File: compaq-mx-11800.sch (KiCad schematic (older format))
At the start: 240 parts, among them J1 Conn_01x16_Female, J2 Conn_01x16_Female

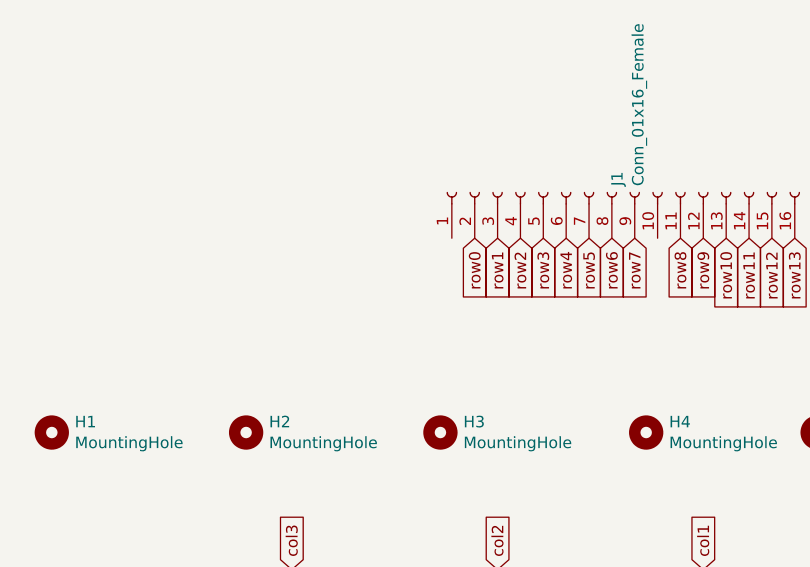
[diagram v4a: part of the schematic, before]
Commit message: add filled zones
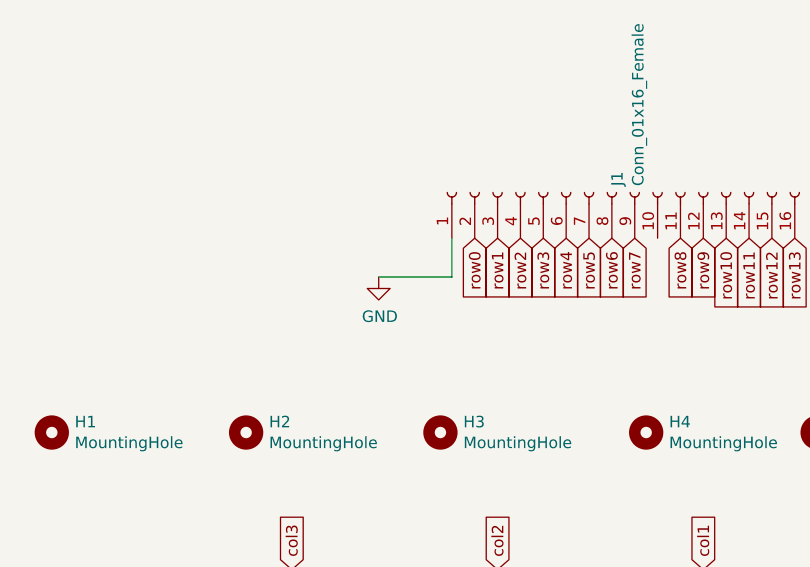
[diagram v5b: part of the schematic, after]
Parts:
- MX1, MX10, MX11, MX12, MX17, MX18, MX19, MX2, MX20, MX21, MX22, MX23, MX24, MX25, MX26, MX27, MX3, MX4, MX5, MX6, MX7, MX8, MX9: footprint MX_Only:MXOnly-1U-NoLED -> MX_Alps_Hybrid:MX-1U-NoLED
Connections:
- net labels added: GND
- wire segments 776 -> 778
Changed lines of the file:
@@
 F 0 "MX1" H 9083 8323 60  0000 C CNN
 F 1 "MX-NoLED" H 9083 8249 20  0000 C CNN
-F 2 "MX_Only:MXOnly-1U-NoLED" H 8425 8075 60  0001 C CNN
+F 2 "MX_Alps_Hybrid:MX-1U-NoLED" H 8425 8075 60  0001 C CNN
 F 3 "" H 8425 8075 60  0001 C CNN
 	1    9050 8100
@@
 F 0 "MX20" H 10883 9123 60  0000 C CNN
 F 1 "MX-NoLED" H 10883 9049 20  0000 C CNN
-F 2 "MX_Only:MXOnly-1U-NoLED" H 10225 8875 60  0001 C CNN
+F 2 "MX_Alps_Hybrid:MX-1U-NoLED" H 10225 8875 60  0001 C CNN
 F 3 "" H 10225 8875 60  0001 C CNN
 	1    10850 8900
@@
 F 0 "MX19" H 10433 9123 60  0000 C CNN
 F 1 "MX-NoLED" H 10433 9049 20  0000 C CNN
-F 2 "MX_Only:MXOnly-1U-NoLED" H 9775 8875 60  0001 C CNN
+F 2 "MX_Alps_Hybrid:MX-1U-NoLED" H 9775 8875 60  0001 C CNN
 F 3 "" H 9775 8875 60  0001 C CNN
 	1    10400 8900
@@
 F 0 "MX18" H 9983 9123 60  0000 C CNN
 F 1 "MX-NoLED" H 9983 9049 20  0000 C CNN
-F 2 "MX_Only:MXOnly-1U-NoLED" H 9325 8875 60  0001 C CNN
+F 2 "MX_Alps_Hybrid:MX-1U-NoLED" H 9325 8875 60  0001 C CNN
 F 3 "" H 9325 8875 60  0001 C CNN
 	1    9950 8900
@@
 F 0 "MX4" H 10883 8323 60  0000 C CNN
 F 1 "MX-NoLED" H 10883 8249 20  0000 C CNN
-F 2 "MX_Only:MXOnly-1U-NoLED" H 10225 8075 60  0001 C CNN
+F 2 "MX_Alps_Hybrid:MX-1U-NoLED" H 10225 8075 60  0001 C CNN
 F 3 "" H 10225 8075 60  0001 C CNN
 	1    10850 8100
@@
 F 0 "MX3" H 10433 8323 60  0000 C CNN
 F 1 "MX-NoLED" H 10433 8249 20  0000 C CNN
-F 2 "MX_Only:MXOnly-1U-NoLED" H 9775 8075 60  0001 C CNN
+F 2 "MX_Alps_Hybrid:MX-1U-NoLED" H 9775 8075 60  0001 C CNN
 F 3 "" H 9775 8075 60  0001 C CNN
 	1    10400 8100
@@
 F 0 "MX2" H 9983 8323 60  0000 C CNN
 F 1 "MX-NoLED" H 9983 8249 20  0000 C CNN
-F 2 "MX_Only:MXOnly-1U-NoLED" H 9325 8075 60  0001 C CNN
+F 2 "MX_Alps_Hybrid:MX-1U-NoLED" H 9325 8075 60  0001 C CNN
 F 3 "" H 9325 8075 60  0001 C CNN
 	1    9950 8100
@@
 F 0 "MX5" H 11333 8323 60  0000 C CNN
 F 1 "MX-NoLED" H 11333 8249 20  0000 C CNN
-F 2 "MX_Only:MXOnly-1U-NoLED" H 10675 8075 60  0001 C CNN
+F 2 "MX_Alps_Hybrid:MX-1U-NoLED" H 10675 8075 60  0001 C CNN
 F 3 "" H 10675 8075 60  0001 C CNN
 	1    11300 8100
@@
 F 0 "MX6" H 11783 8323 60  0000 C CNN
 F 1 "MX-NoLED" H 11783 8249 20  0000 C CNN
-F 2 "MX_Only:MXOnly-1U-NoLED" H 11125 8075 60  0001 C CNN
+F 2 "MX_Alps_Hybrid:MX-1U-NoLED" H 11125 8075 60  0001 C CNN
 F 3 "" H 11125 8075 60  0001 C CNN
 	1    11750 8100
@@
 F 0 "MX7" H 12233 8323 60  0000 C CNN
 F 1 "MX-NoLED" H 12233 8249 20  0000 C CNN
-F 2 "MX_Only:MXOnly-1U-NoLED" H 11575 8075 60  0001 C CNN
+F 2 "MX_Alps_Hybrid:MX-1U-NoLED" H 11575 8075 60  0001 C CNN
 F 3 "" H 11575 8075 60  0001 C CNN
 	1    12200 8100
@@
 F 0 "MX8" H 13133 8323 60  0000 C CNN
 F 1 "MX-NoLED" H 13133 8249 20  0000 C CNN
-F 2 "MX_Only:MXOnly-1U-NoLED" H 12475 8075 60  0001 C CNN
+F 2 "MX_Alps_Hybrid:MX-1U-NoLED" H 12475 8075 60  0001 C CNN
 F 3 "" H 12475 8075 60  0001 C CNN
 	1    13100 8100
@@
 F 0 "MX9" H 13583 8323 60  0000 C CNN
 F 1 "MX-NoLED" H 13583 8249 20  0000 C CNN
-F 2 "MX_Only:MXOnly-1U-NoLED" H 12925 8075 60  0001 C CNN
+F 2 "MX_Alps_Hybrid:MX-1U-NoLED" H 12925 8075 60  0001 C CNN
 F 3 "" H 12925 8075 60  0001 C CNN
 	1    13550 8100
@@
 F 0 "MX21" H 11333 9123 60  0000 C CNN
 F 1 "MX-NoLED" H 11333 9049 20  0000 C CNN
-F 2 "MX_Only:MXOnly-1U-NoLED" H 10675 8875 60  0001 C CNN
+F 2 "MX_Alps_Hybrid:MX-1U-NoLED" H 10675 8875 60  0001 C CNN
 F 3 "" H 10675 8875 60  0001 C CNN
 	1    11300 8900
@@
 F 0 "MX22" H 11783 9123 60  0000 C CNN
 F 1 "MX-NoLED" H 11783 9049 20  0000 C CNN
-F 2 "MX_Only:MXOnly-1U-NoLED" H 11125 8875 60  0001 C CNN
+F 2 "MX_Alps_Hybrid:MX-1U-NoLED" H 11125 8875 60  0001 C CNN
 F 3 "" H 11125 8875 60  0001 C CNN
 	1    11750 8900
@@
 F 0 "MX23" H 12233 9123 60  0000 C CNN
 F 1 "MX-NoLED" H 12233 9049 20  0000 C CNN
-F 2 "MX_Only:MXOnly-1U-NoLED" H 11575 8875 60  0001 C CNN
+F 2 "MX_Alps_Hybrid:MX-1U-NoLED" H 11575 8875 60  0001 C CNN
 F 3 "" H 11575 8875 60  0001 C CNN
 	1    12200 8900
@@
 F 0 "MX24" H 13133 9123 60  0000 C CNN
 F 1 "MX-NoLED" H 13133 9049 20  0000 C CNN
-F 2 "MX_Only:MXOnly-1U-NoLED" H 12475 8875 60  0001 C CNN
+F 2 "MX_Alps_Hybrid:MX-1U-NoLED" H 12475 8875 60  0001 C CNN
 F 3 "" H 12475 8875 60  0001 C CNN
 	1    13100 8900
@@
 F 0 "MX25" H 13583 9123 60  0000 C CNN
 F 1 "MX-NoLED" H 13583 9049 20  0000 C CNN
-F 2 "MX_Only:MXOnly-1U-NoLED" H 12925 8875 60  0001 C CNN
+F 2 "MX_Alps_Hybrid:MX-1U-NoLED" H 12925 8875 60  0001 C CNN
 F 3 "" H 12925 8875 60  0001 C CNN
 	1    13550 8900
@@
 F 0 "MX26" H 14033 9123 60  0000 C CNN
 F 1 "MX-NoLED" H 14033 9049 20  0000 C CNN
-F 2 "MX_Only:MXOnly-1U-NoLED" H 13375 8875 60  0001 C CNN
+F 2 "MX_Alps_Hybrid:MX-1U-NoLED" H 13375 8875 60  0001 C CNN
 F 3 "" H 13375 8875 60  0001 C CNN
 	1    14000 8900
@@
 F 0 "MX10" H 14033 8323 60  0000 C CNN
 F 1 "MX-NoLED" H 14033 8249 20  0000 C CNN
-F 2 "MX_Only:MXOnly-1U-NoLED" H 13375 8075 60  0001 C CNN
+F 2 "MX_Alps_Hybrid:MX-1U-NoLED" H 13375 8075 60  0001 C CNN
 F 3 "" H 13375 8075 60  0001 C CNN
 	1    14000 8100
@@
 F 0 "MX11" H 14483 8323 60  0000 C CNN
 F 1 "MX-NoLED" H 14483 8249 20  0000 C CNN
-F 2 "MX_Only:MXOnly-1U-NoLED" H 13825 8075 60  0001 C CNN
+F 2 "MX_Alps_Hybrid:MX-1U-NoLED" H 13825 8075 60  0001 C CNN
 F 3 "" H 13825 8075 60  0001 C CNN
 	1    14450 8100
@@
 F 0 "MX27" H 14483 9123 60  0000 C CNN
 F 1 "MX-NoLED" H 14483 9049 20  0000 C CNN
-F 2 "MX_Only:MXOnly-1U-NoLED" H 13825 8875 60  0001 C CNN
+F 2 "MX_Alps_Hybrid:MX-1U-NoLED" H 13825 8875 60  0001 C CNN
 F 3 "" H 13825 8875 60  0001 C CNN
 	1    14450 8900
@@
 F 0 "MX12" H 14983 8323 60  0000 C CNN
 F 1 "MX-NoLED" H 14983 8249 20  0000 C CNN
-F 2 "MX_Only:MXOnly-1U-NoLED" H 14325 8075 60  0001 C CNN
+F 2 "MX_Alps_Hybrid:MX-1U-NoLED" H 14325 8075 60  0001 C CNN
 F 3 "" H 14325 8075 60  0001 C CNN
 	1    14950 8100
@@
 F 0 "MX17" H 18283 9273 60  0000 C CNN
 F 1 "MX-NoLED" H 18283 9199 20  0000 C CNN
-F 2 "MX_Only:MXOnly-1U-NoLED" H 17625 9025 60  0001 C CNN
+F 2 "MX_Alps_Hybrid:MX-1U-NoLED" H 17625 9025 60  0001 C CNN
 F 3 "" H 17625 9025 60  0001 C CNN
 	1    18250 9050
@@
 Wire Wire Line
 	8900 11100 8900 11200
+$Comp
+L power:GND #PWR0101
+U 1 1 61E256F8
+P 9630 6470
+F 0 "#PWR0101" H 9630 6220 50  0001 C CNN
+F 1 "GND" H 9635 6297 50  0000 C CNN
+F 2 "" H 9630 6470 50  0001 C CNN
+F 3 "" H 9630 6470 50  0001 C CNN
+	1    9630 6470
+	1    0    0    -1
+$EndComp
+Wire Wire Line
+	9950 6300 9950 6470
+Wire Wire Line
+	9950 6470 9630 6470
 $EndSCHEMATC

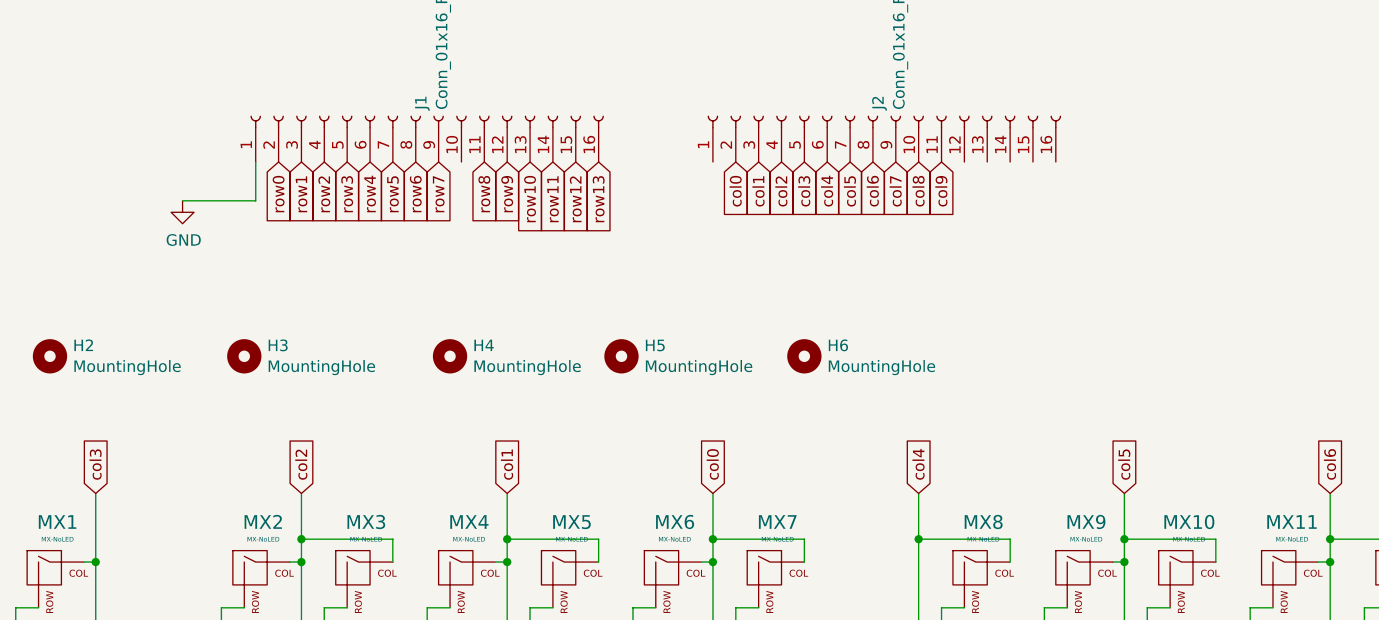
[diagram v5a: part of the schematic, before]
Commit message: add ground pins
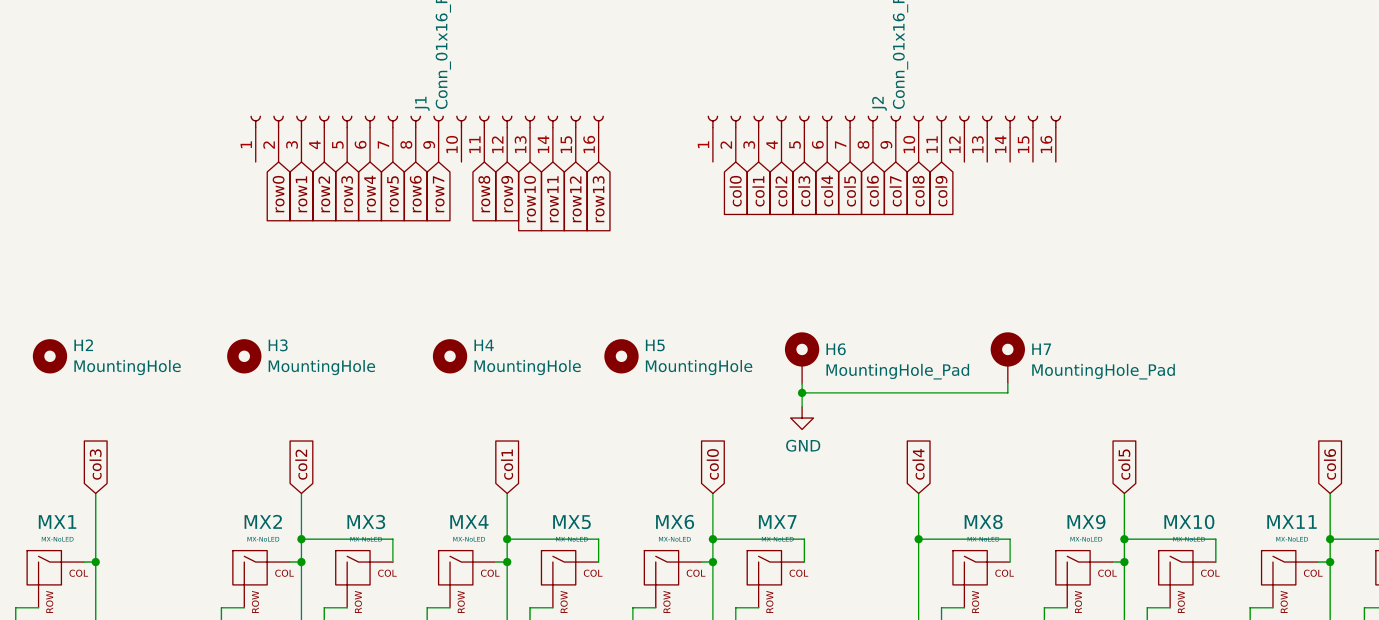
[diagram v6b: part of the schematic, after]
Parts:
- removed H6: MountingHole, Keebio-Parts:SolidCopper, symbol Mechanical:MountingHole
- added H6, H7: MountingHole_Pad, Keebio-Parts:SolidCopper, symbol Mechanical:MountingHole_Pad
- MX1, MX10, MX11, MX12, MX17, MX18, MX19, MX2, MX20, MX21, MX22, MX23, MX24, MX25, MX26, MX27, MX3, MX4, MX5, MX6, MX7, MX8, MX9: footprint MX_Alps_Hybrid:MX-1U-NoLED -> MX_Only:MXOnly-1U-NoLED
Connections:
- wire segments 778 -> 780
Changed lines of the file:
@@
 F 0 "MX1" H 9083 8323 60  0000 C CNN
 F 1 "MX-NoLED" H 9083 8249 20  0000 C CNN
-F 2 "MX_Alps_Hybrid:MX-1U-NoLED" H 8425 8075 60  0001 C CNN
+F 2 "MX_Only:MXOnly-1U-NoLED" H 8425 8075 60  0001 C CNN
 F 3 "" H 8425 8075 60  0001 C CNN
 	1    9050 8100
@@
 F 0 "MX20" H 10883 9123 60  0000 C CNN
 F 1 "MX-NoLED" H 10883 9049 20  0000 C CNN
-F 2 "MX_Alps_Hybrid:MX-1U-NoLED" H 10225 8875 60  0001 C CNN
+F 2 "MX_Only:MXOnly-1U-NoLED" H 10225 8875 60  0001 C CNN
 F 3 "" H 10225 8875 60  0001 C CNN
 	1    10850 8900
@@
 F 0 "MX19" H 10433 9123 60  0000 C CNN
 F 1 "MX-NoLED" H 10433 9049 20  0000 C CNN
-F 2 "MX_Alps_Hybrid:MX-1U-NoLED" H 9775 8875 60  0001 C CNN
+F 2 "MX_Only:MXOnly-1U-NoLED" H 9775 8875 60  0001 C CNN
 F 3 "" H 9775 8875 60  0001 C CNN
 	1    10400 8900
@@
 F 0 "MX18" H 9983 9123 60  0000 C CNN
 F 1 "MX-NoLED" H 9983 9049 20  0000 C CNN
-F 2 "MX_Alps_Hybrid:MX-1U-NoLED" H 9325 8875 60  0001 C CNN
+F 2 "MX_Only:MXOnly-1U-NoLED" H 9325 8875 60  0001 C CNN
 F 3 "" H 9325 8875 60  0001 C CNN
 	1    9950 8900
@@
 F 0 "MX4" H 10883 8323 60  0000 C CNN
 F 1 "MX-NoLED" H 10883 8249 20  0000 C CNN
-F 2 "MX_Alps_Hybrid:MX-1U-NoLED" H 10225 8075 60  0001 C CNN
+F 2 "MX_Only:MXOnly-1U-NoLED" H 10225 8075 60  0001 C CNN
 F 3 "" H 10225 8075 60  0001 C CNN
 	1    10850 8100
@@
 F 0 "MX3" H 10433 8323 60  0000 C CNN
 F 1 "MX-NoLED" H 10433 8249 20  0000 C CNN
-F 2 "MX_Alps_Hybrid:MX-1U-NoLED" H 9775 8075 60  0001 C CNN
+F 2 "MX_Only:MXOnly-1U-NoLED" H 9775 8075 60  0001 C CNN
 F 3 "" H 9775 8075 60  0001 C CNN
 	1    10400 8100
@@
 F 0 "MX2" H 9983 8323 60  0000 C CNN
 F 1 "MX-NoLED" H 9983 8249 20  0000 C CNN
-F 2 "MX_Alps_Hybrid:MX-1U-NoLED" H 9325 8075 60  0001 C CNN
+F 2 "MX_Only:MXOnly-1U-NoLED" H 9325 8075 60  0001 C CNN
 F 3 "" H 9325 8075 60  0001 C CNN
 	1    9950 8100
@@
 F 0 "MX5" H 11333 8323 60  0000 C CNN
 F 1 "MX-NoLED" H 11333 8249 20  0000 C CNN
-F 2 "MX_Alps_Hybrid:MX-1U-NoLED" H 10675 8075 60  0001 C CNN
+F 2 "MX_Only:MXOnly-1U-NoLED" H 10675 8075 60  0001 C CNN
 F 3 "" H 10675 8075 60  0001 C CNN
 	1    11300 8100
@@
 F 0 "MX6" H 11783 8323 60  0000 C CNN
 F 1 "MX-NoLED" H 11783 8249 20  0000 C CNN
-F 2 "MX_Alps_Hybrid:MX-1U-NoLED" H 11125 8075 60  0001 C CNN
+F 2 "MX_Only:MXOnly-1U-NoLED" H 11125 8075 60  0001 C CNN
 F 3 "" H 11125 8075 60  0001 C CNN
 	1    11750 8100
@@
 F 0 "MX7" H 12233 8323 60  0000 C CNN
 F 1 "MX-NoLED" H 12233 8249 20  0000 C CNN
-F 2 "MX_Alps_Hybrid:MX-1U-NoLED" H 11575 8075 60  0001 C CNN
+F 2 "MX_Only:MXOnly-1U-NoLED" H 11575 8075 60  0001 C CNN
 F 3 "" H 11575 8075 60  0001 C CNN
 	1    12200 8100
@@
 F 0 "MX8" H 13133 8323 60  0000 C CNN
 F 1 "MX-NoLED" H 13133 8249 20  0000 C CNN
-F 2 "MX_Alps_Hybrid:MX-1U-NoLED" H 12475 8075 60  0001 C CNN
+F 2 "MX_Only:MXOnly-1U-NoLED" H 12475 8075 60  0001 C CNN
 F 3 "" H 12475 8075 60  0001 C CNN
 	1    13100 8100
@@
 F 0 "MX9" H 13583 8323 60  0000 C CNN
 F 1 "MX-NoLED" H 13583 8249 20  0000 C CNN
-F 2 "MX_Alps_Hybrid:MX-1U-NoLED" H 12925 8075 60  0001 C CNN
+F 2 "MX_Only:MXOnly-1U-NoLED" H 12925 8075 60  0001 C CNN
 F 3 "" H 12925 8075 60  0001 C CNN
 	1    13550 8100
@@
 F 0 "MX21" H 11333 9123 60  0000 C CNN
 F 1 "MX-NoLED" H 11333 9049 20  0000 C CNN
-F 2 "MX_Alps_Hybrid:MX-1U-NoLED" H 10675 8875 60  0001 C CNN
+F 2 "MX_Only:MXOnly-1U-NoLED" H 10675 8875 60  0001 C CNN
 F 3 "" H 10675 8875 60  0001 C CNN
 	1    11300 8900
@@
 F 0 "MX22" H 11783 9123 60  0000 C CNN
 F 1 "MX-NoLED" H 11783 9049 20  0000 C CNN
-F 2 "MX_Alps_Hybrid:MX-1U-NoLED" H 11125 8875 60  0001 C CNN
+F 2 "MX_Only:MXOnly-1U-NoLED" H 11125 8875 60  0001 C CNN
 F 3 "" H 11125 8875 60  0001 C CNN
 	1    11750 8900
@@
 F 0 "MX23" H 12233 9123 60  0000 C CNN
 F 1 "MX-NoLED" H 12233 9049 20  0000 C CNN
-F 2 "MX_Alps_Hybrid:MX-1U-NoLED" H 11575 8875 60  0001 C CNN
+F 2 "MX_Only:MXOnly-1U-NoLED" H 11575 8875 60  0001 C CNN
 F 3 "" H 11575 8875 60  0001 C CNN
 	1    12200 8900
@@
 F 0 "MX24" H 13133 9123 60  0000 C CNN
 F 1 "MX-NoLED" H 13133 9049 20  0000 C CNN
-F 2 "MX_Alps_Hybrid:MX-1U-NoLED" H 12475 8875 60  0001 C CNN
+F 2 "MX_Only:MXOnly-1U-NoLED" H 12475 8875 60  0001 C CNN
 F 3 "" H 12475 8875 60  0001 C CNN
 	1    13100 8900
@@
 F 0 "MX25" H 13583 9123 60  0000 C CNN
 F 1 "MX-NoLED" H 13583 9049 20  0000 C CNN
-F 2 "MX_Alps_Hybrid:MX-1U-NoLED" H 12925 8875 60  0001 C CNN
+F 2 "MX_Only:MXOnly-1U-NoLED" H 12925 8875 60  0001 C CNN
 F 3 "" H 12925 8875 60  0001 C CNN
 	1    13550 8900
@@
 F 0 "MX26" H 14033 9123 60  0000 C CNN
 F 1 "MX-NoLED" H 14033 9049 20  0000 C CNN
-F 2 "MX_Alps_Hybrid:MX-1U-NoLED" H 13375 8875 60  0001 C CNN
+F 2 "MX_Only:MXOnly-1U-NoLED" H 13375 8875 60  0001 C CNN
 F 3 "" H 13375 8875 60  0001 C CNN
 	1    14000 8900
@@
 F 0 "MX10" H 14033 8323 60  0000 C CNN
 F 1 "MX-NoLED" H 14033 8249 20  0000 C CNN
-F 2 "MX_Alps_Hybrid:MX-1U-NoLED" H 13375 8075 60  0001 C CNN
+F 2 "MX_Only:MXOnly-1U-NoLED" H 13375 8075 60  0001 C CNN
 F 3 "" H 13375 8075 60  0001 C CNN
 	1    14000 8100
@@
 F 0 "MX11" H 14483 8323 60  0000 C CNN
 F 1 "MX-NoLED" H 14483 8249 20  0000 C CNN
-F 2 "MX_Alps_Hybrid:MX-1U-NoLED" H 13825 8075 60  0001 C CNN
+F 2 "MX_Only:MXOnly-1U-NoLED" H 13825 8075 60  0001 C CNN
 F 3 "" H 13825 8075 60  0001 C CNN
 	1    14450 8100
@@
 F 0 "MX27" H 14483 9123 60  0000 C CNN
 F 1 "MX-NoLED" H 14483 9049 20  0000 C CNN
-F 2 "MX_Alps_Hybrid:MX-1U-NoLED" H 13825 8875 60  0001 C CNN
+F 2 "MX_Only:MXOnly-1U-NoLED" H 13825 8875 60  0001 C CNN
 F 3 "" H 13825 8875 60  0001 C CNN
 	1    14450 8900
@@
 F 0 "MX12" H 14983 8323 60  0000 C CNN
 F 1 "MX-NoLED" H 14983 8249 20  0000 C CNN
-F 2 "MX_Alps_Hybrid:MX-1U-NoLED" H 14325 8075 60  0001 C CNN
+F 2 "MX_Only:MXOnly-1U-NoLED" H 14325 8075 60  0001 C CNN
 F 3 "" H 14325 8075 60  0001 C CNN
 	1    14950 8100
@@
 	9250 8050 9250 9950
 $Comp
-L Mechanical:MountingHole H6
-U 1 1 61D29BE7
-P 12350 7150
-F 0 "H6" H 12450 7196 50  0000 L CNN
-F 1 "MountingHole" H 12450 7105 50  0000 L CNN
-F 2 "Keebio-Parts:SolidCopper" H 12350 7150 50  0001 C CNN
-F 3 "~" H 12350 7150 50  0001 C CNN
-	1    12350 7150
-	1    0    0    -1
-$EndComp
-$Comp
 L Mechanical:MountingHole H5
 U 1 1 61CD4313
@@
 F 0 "MX17" H 18283 9273 60  0000 C CNN
 F 1 "MX-NoLED" H 18283 9199 20  0000 C CNN
-F 2 "MX_Alps_Hybrid:MX-1U-NoLED" H 17625 9025 60  0001 C CNN
+F 2 "MX_Only:MXOnly-1U-NoLED" H 17625 9025 60  0001 C CNN
 F 3 "" H 17625 9025 60  0001 C CNN
 	1    18250 9050
@@
 	8900 11100 8900 11200
 $Comp
-L power:GND #PWR0101
-U 1 1 61E256F8
-P 9630 6470
-F 0 "#PWR0101" H 9630 6220 50  0001 C CNN
-F 1 "GND" H 9635 6297 50  0000 C CNN
-F 2 "" H 9630 6470 50  0001 C CNN
-F 3 "" H 9630 6470 50  0001 C CNN
-	1    9630 6470
+L Mechanical:MountingHole_Pad H7
+U 1 1 620D9A4A
+P 13240 7170
+F 0 "H7" H 13340 7219 50  0000 L CNN
+F 1 "MountingHole_Pad" H 13340 7128 50  0000 L CNN
+F 2 "Keebio-Parts:SolidCopper" H 13240 7170 50  0001 C CNN
+F 3 "~" H 13240 7170 50  0001 C CNN
+	1    13240 7170
+	1    0    0    -1
+$EndComp
+$Comp
+L power:GND #PWR0102
+U 1 1 62315AC5
+P 12340 7370
+F 0 "#PWR0102" H 12340 7120 50  0001 C CNN
+F 1 "GND" H 12345 7197 50  0000 C CNN
+F 2 "" H 12340 7370 50  0001 C CNN
+F 3 "" H 12340 7370 50  0001 C CNN
+	1    12340 7370
 	1    0    0    -1
 $EndComp
+$Comp
+L Mechanical:MountingHole_Pad H6
+U 1 1 62315ACB
+P 12340 7170
+F 0 "H6" H 12440 7219 50  0000 L CNN
+F 1 "MountingHole_Pad" H 12440 7128 50  0000 L CNN
+F 2 "Keebio-Parts:SolidCopper" H 12340 7170 50  0001 C CNN
+F 3 "~" H 12340 7170 50  0001 C CNN
+	1    12340 7170
+	1    0    0    -1
+$EndComp
+Wire Wire Line
+	12340 7270 12340 7310
+Wire Wire Line
+	13240 7270 13240 7310
 Wire Wire Line
-	9950 6300 9950 6470
+	13240 7310 12340 7310
+Connection ~ 12340 7310
 Wire Wire Line
-	9950 6470 9630 6470
+	12340 7310 12340 7370
 $EndSCHEMATC
